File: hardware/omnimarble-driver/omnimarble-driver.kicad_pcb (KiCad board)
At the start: 4 copper layers, 220 x 150 mm, 177 parts, among them J1 24V-IN, J10 PICO-SOCKET, J2 AUX-BANK, J3 E-STOP-NC, J4 ARM-KEY, J5 COIL, J6 RAIL-EMIT, J7 RAIL-RECV, J8 SPARE-JST, J9 PICO-SOCKET, K1 HF3FF-12V, K2 HF3FF-12V, Q1 MMBT3904, Q10 SFT040N150C3, Q11 SFT040N150C3, Q12 SFT040N150C3, Q2 MMBT3904, Q3 MMBT3904, Q4 MMBT3904, Q90 AOD4185, Q91 AOD66923, U1 AP63205, U10 ADS7042, U11 LM339, U12 LM339, U2 78L12, U3 MCP6002, U4 UC3843B, U5 CJ431-0.5%, U6 74LVC1G08, U7 UCC27524A, U8 UCC27524A, U9 INA240A1

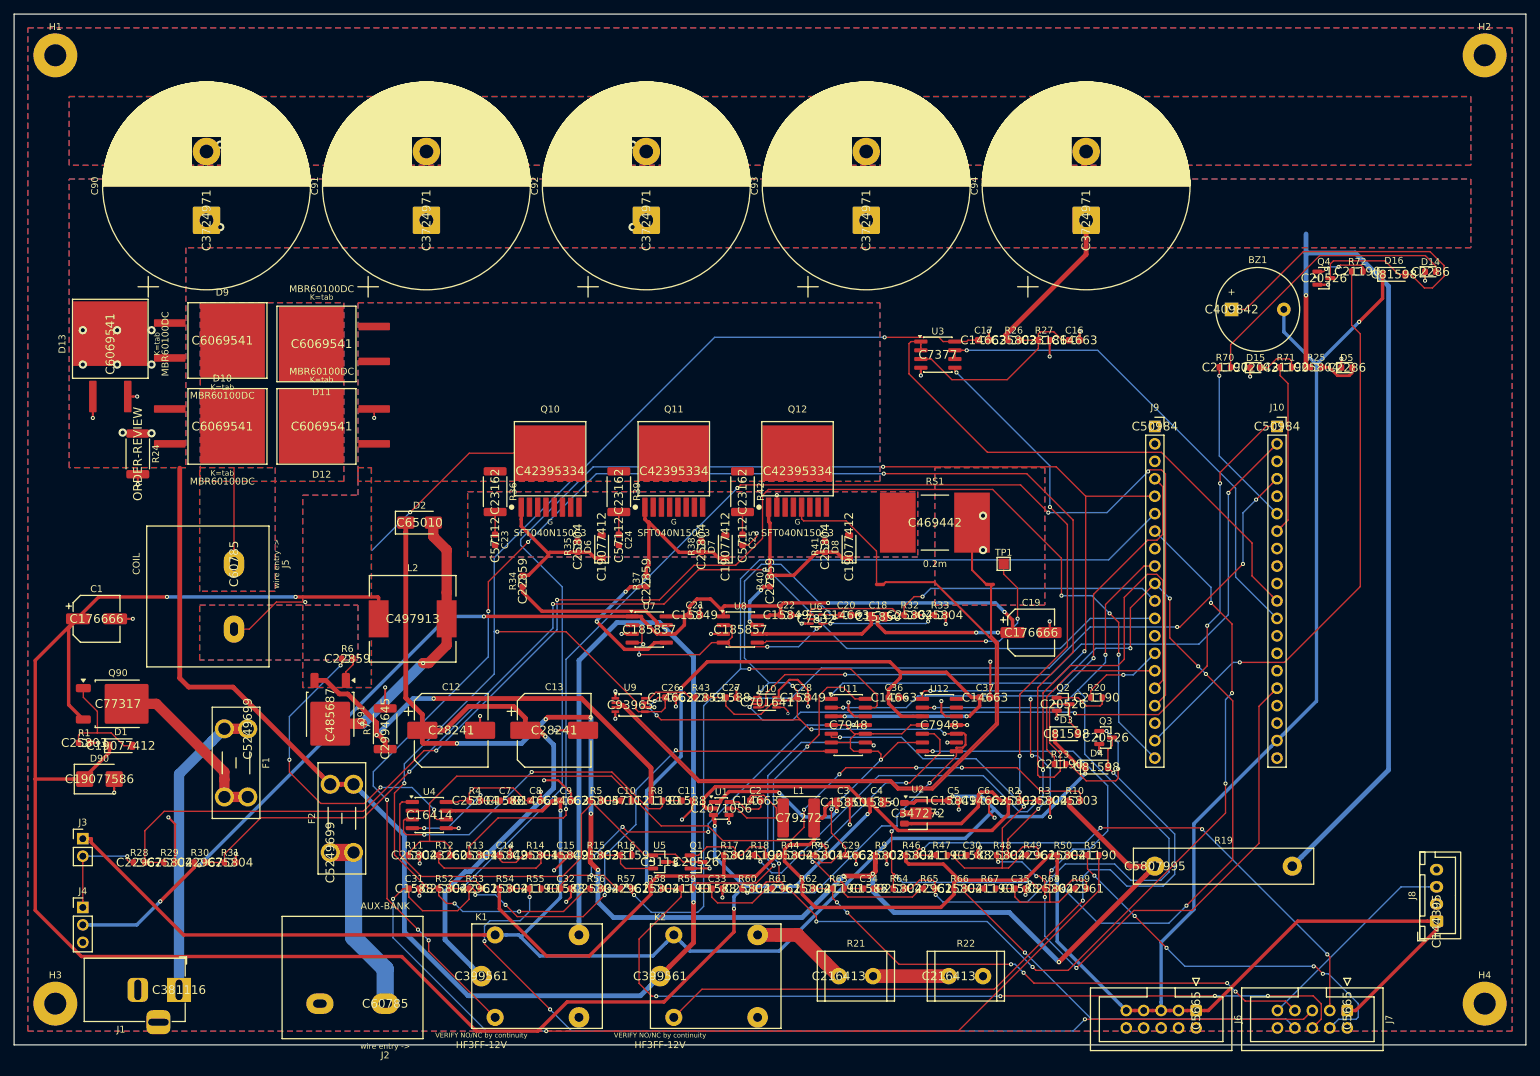
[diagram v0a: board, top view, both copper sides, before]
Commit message: Driver PCB: author SHUNT_HI B.Cu bus + dedicated ISNS diff-pair class (fresh route prep)
Prep for one clean full re-route with every learned fix baked in:
- author_shunt_hi_bus(): explicit locked B.Cu bus tying all 3 pulse-FET sources
  (Q10/Q11/Q12) + shunt RS1, 2 vias per multi-pad source. The SHUNT_HI current
  path no longer depends on the F.Cu pour (which the router fragments); B.Cu
  keeps F.Cu clear for gate routing. Fixes the recurring Q10/Q11 islanding.
- diff_ISNS net class (ISNS_P/ISNS_N, 0.3mm/0.2mm gap): prefetches the diff pair
  DeepPCB always asks about, pre-set to our 0.2mm clearance so its coupling
  can't come back at the unmanufacturable 0.02mm, and passes DRC with no
  exception rule.
Everything else already baked: 3V3=0.2mm, U10 dogbone escape (locked), no GND
via-in-pad (DeepPCB does GND->plane), sanitized net names, widths fit pads,
annular auto-patched at import. DSN verified clean.

Co-Authored-By: Claude Fable 5 <noreply@anthropic.com>
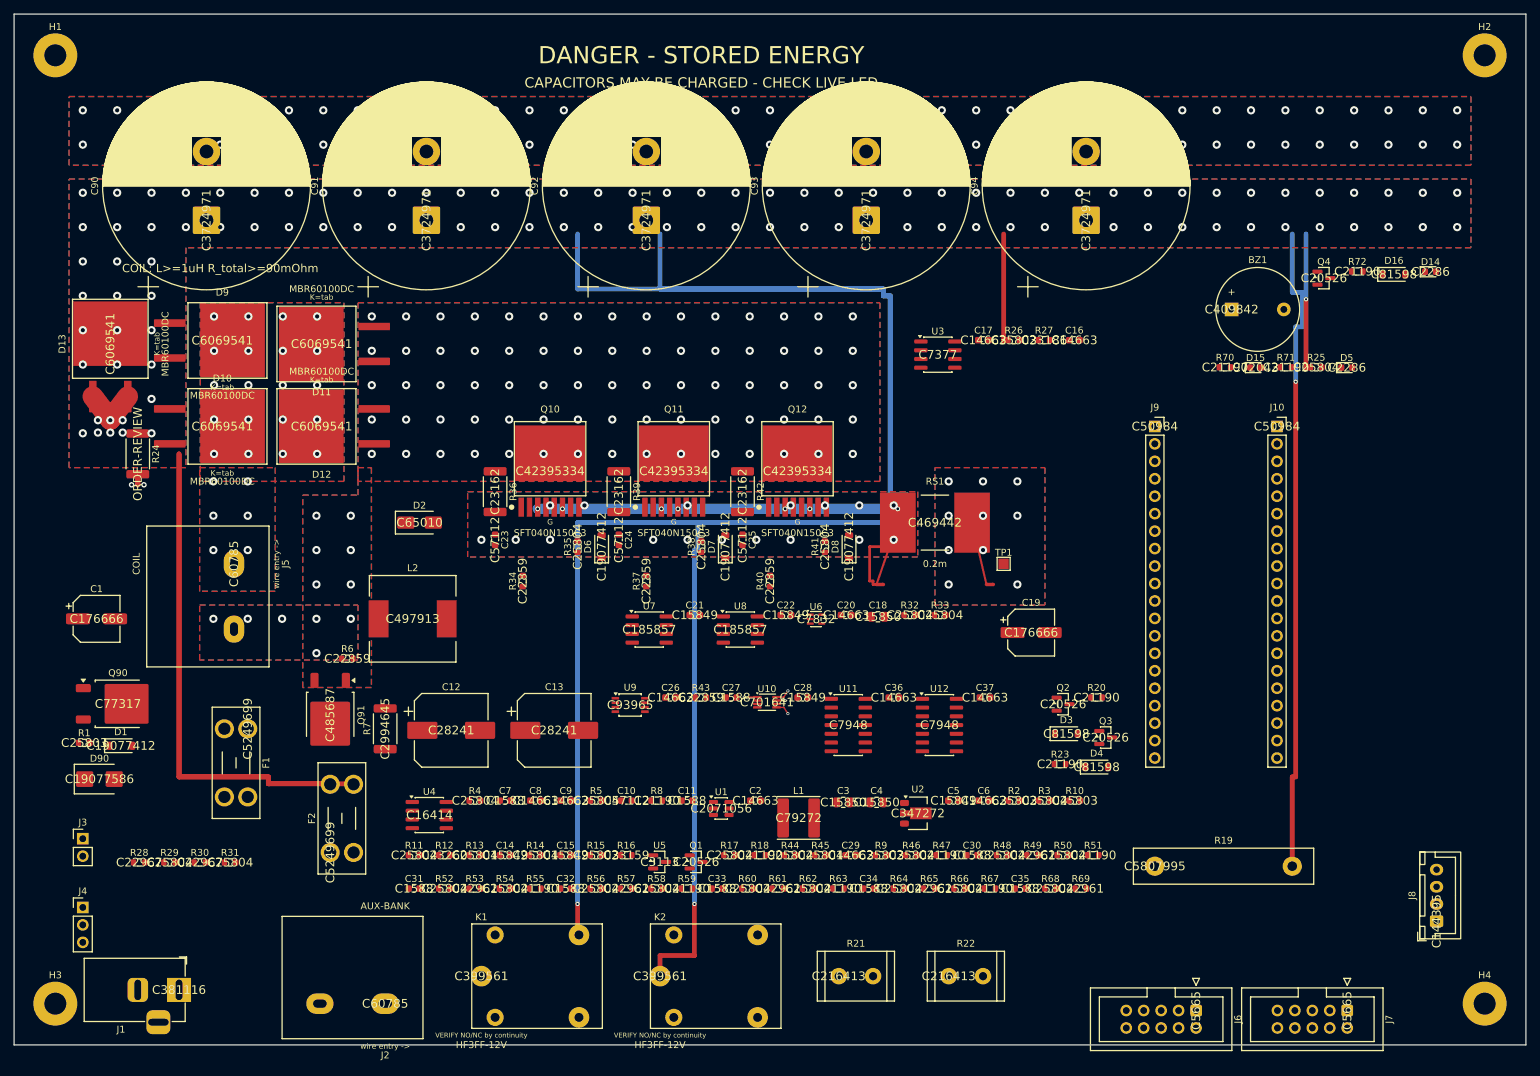
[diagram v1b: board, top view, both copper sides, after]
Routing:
- net +5V: track 491.7 -> 0.00 mm, vias 8 -> 0
- net 3V3: track 458.4 -> 3.15 mm, vias 21 -> 2
- net +24V: track 352.5 -> 0.00 mm, vias 5 -> 0
- net VBANK: track 383.9 -> 655.2 mm, vias 12 -> 99
- net VBOOST: track 269.5 -> 0.00 mm, vias 9 -> 0
- net K1_COIL: track 232.1 -> 0.00 mm, vias 6 -> 0
- net +12V: track 228.9 -> 0.00 mm, vias 3 -> 0
- net GATE2: track 227.8 -> 0.00 mm, vias 4 -> 0
- net CIN2: track 214.7 -> 0.00 mm, vias 6 -> 0
- net +12V_SW: track 212.3 -> 0.00 mm, vias 7 -> 0
- net ESTOP_SENSE: track 208.5 -> 0.00 mm, vias 5 -> 0
- net VSET_PWM: track 176.5 -> 0.00 mm, vias 4 -> 0
- net GATE4: track 169.1 -> 0.00 mm, vias 7 -> 0
- net ARM_SENSE: track 165.7 -> 0.00 mm, vias 4 -> 0
- net GATE3: track 156.3 -> 0.00 mm, vias 4 -> 0
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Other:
- board text added: "CAPACITORS MAY BE CHARGED - CHECK LIVE LED"
- board text added: "COIL: L>=1uH R_total>=90mOhm"
- board text added: "DANGER - STORED ENERGY"
